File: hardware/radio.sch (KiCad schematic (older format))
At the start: 80 parts, among them J1 JCLK, P2 JLED1, U1 G144A12, U3V3t1V8 NCP1117ST18T3G, U5V0t3V3 NCP1117ST33T3G

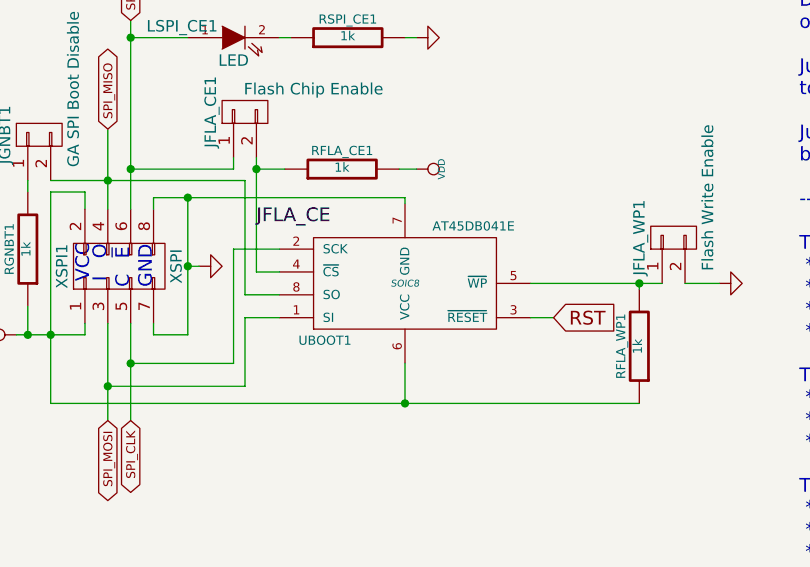
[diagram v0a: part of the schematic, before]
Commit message: Adding SATA PCB module.
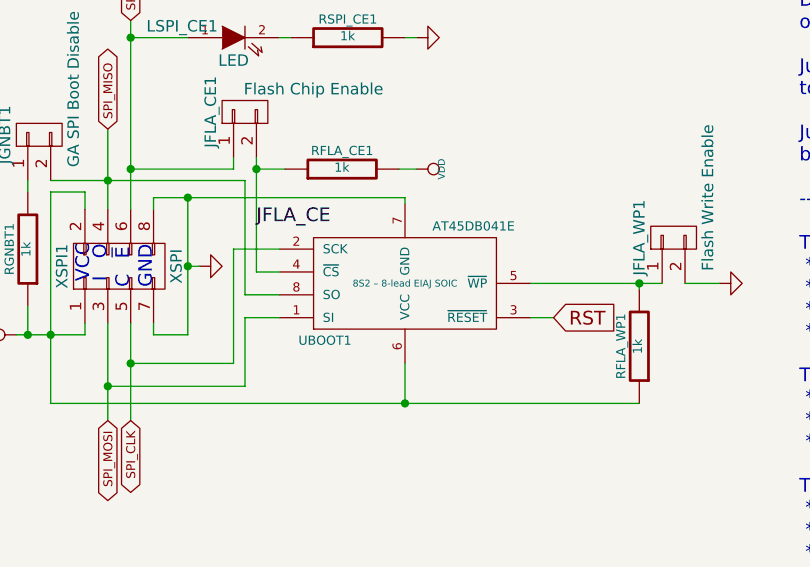
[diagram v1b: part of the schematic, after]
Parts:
- AN2: footprint (none) -> Pin_Headers:Pin_Header_Straight_1x03
- CPWR1: footprint (none) -> Connect:BARREL_JACK
- JFLA_CE1, JFLA_WP1, JGNBT1: footprint (none) -> Pin_Headers:Pin_Header_Straight_1x02
- RFLA_CE1, RFLA_WP1, RGNBT1, RLB1, ROE1, RSPI_CE1, RUB1: footprint (none) -> Resistors_SMD:R_0603
- U5V0t3V3: footprint (none) -> SMD_Packages:SOT-223
- UBOOT1: footprint SOIC8 -> SMD_Packages:SOIC-8-N
- XMEM1: footprint (none) -> tssop2-44:TSSOPII-44_0.8mmPitch
- XSPI1: footprint (none) -> Pin_Headers:Pin_Header_Straight_1x04
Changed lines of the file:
@@
 F 0 "XSPI1" H 6525 15525 50  0000 C CNN
 F 1 "XSPI" H 6525 15025 50  0000 C CNN
-F 2 "" H 6525 14075 60  0000 C CNN
+F 2 "Pin_Headers:Pin_Header_Straight_1x04" H 6525 14075 60  0001 C CNN
 F 3 "" H 6525 14075 60  0000 C CNN
 	1    6525 15275
@@
 F 0 "UBOOT1" H 7425 15600 40  0000 C CNN
 F 1 "AT45DB041E" H 8075 15100 40  0000 C CNN
-F 2 "SOIC8" H 7775 15350 30  0000 C CIN
-F 3 "" H 7775 15350 60  0000 C CNN
+F 2 "SMD_Packages:SOIC-8-N" H 7775 15350 30  0001 C CIN
+F 3 "8S2 – 8-lead EIAJ SOIC" H 7775 15350 30  0000 C CNN
 	1    7775 15350
 	1    0    0    1
@@
 F 0 "JFLA_WP1" H 8950 15300 50  0000 C CNN
 F 1 "Flash Write Enable" H 9125 15000 50  0000 C CNN
-F 2 "" H 8950 15150 60  0000 C CNN
+F 2 "Pin_Headers:Pin_Header_Straight_1x02" H 8950 15150 60  0001 C CNN
 F 3 "" H 8950 15150 60  0000 C CNN
 	1    8950 15150
@@
 F 0 "RFLA_WP1" V 8880 15625 40  0000 C CNN
 F 1 "1k" V 8807 15626 40  0000 C CNN
-F 2 "" V 8730 15625 30  0000 C CNN
+F 2 "Resistors_SMD:R_0603" V 8730 15625 30  0001 C CNN
 F 3 "" H 8800 15625 30  0000 C CNN
 	1    8800 15625
@@
 F 0 "AN2" H 30275 6900 50  0000 C CNN
 F 1 "CONN_01X03" V 30375 6700 50  0000 C CNN
-F 2 "" H 30275 6700 60  0000 C CNN
+F 2 "Pin_Headers:Pin_Header_Straight_1x03" H 30275 6700 60  0001 C CNN
 F 3 "" H 30275 6700 60  0000 C CNN
 	1    30275 6700
@@
 F 0 "CPWR1" H 28100 5750 60  0000 C CNN
 F 1 "BARREL_JACK" H 28100 5300 60  0000 C CNN
-F 2 "" H 28100 5500 60  0000 C CNN
+F 2 "Connect:BARREL_JACK" H 28100 5500 60  0001 C CNN
 F 3 "" H 28100 5500 60  0000 C CNN
 	1    28100 5500
@@
 F 0 "U5V0t3V3" H 26975 5700 40  0000 C CNN
 F 1 "NCP1117ST33T3G" H 26975 5650 40  0000 C CNN
-F 2 "" H 26975 5450 60  0000 C CNN
+F 2 "SMD_Packages:SOT-223" H 26975 5450 60  0001 C CNN
 F 3 "" H 26975 5450 60  0000 C CNN
 	1    26975 5450
@@
 F 0 "XMEM1" H 4500 8250 50  0000 C CNN
 F 1 "IS62/65WV51216E(A|B)LL" V 4500 7100 50  0000 C CNN
-F 2 "" H 4500 6200 60  0000 C CNN
+F 2 "tssop2-44:TSSOPII-44_0.8mmPitch" H 4500 6200 60  0001 C CNN
 F 3 "" H 4500 6200 60  0000 C CNN
 	1    4500 7100
@@
 F 0 "RUB1" V 5125 8600 40  0000 C CNN
 F 1 "1K" V 5082 8851 40  0000 C CNN
-F 2 "" V 5005 8850 30  0000 C CNN
+F 2 "Resistors_SMD:R_0603" V 5005 8850 30  0001 C CNN
 F 3 "" H 5075 8850 30  0000 C CNN
 	1    5075 8850
@@
 F 0 "RLB1" V 5125 8700 40  0000 C CNN
 F 1 "1K" V 5082 8951 40  0000 C CNN
-F 2 "" V 5005 8950 30  0000 C CNN
+F 2 "Resistors_SMD:R_0603" V 5005 8950 30  0001 C CNN
 F 3 "" H 5075 8950 30  0000 C CNN
 	1    5075 8950
@@
 F 0 "ROE1" V 5125 8500 40  0000 C CNN
 F 1 "1K" V 5082 8751 40  0000 C CNN
-F 2 "" V 5005 8750 30  0000 C CNN
+F 2 "Resistors_SMD:R_0603" V 5005 8750 30  0001 C CNN
 F 3 "" H 5075 8750 30  0000 C CNN
 	1    5075 8750
@@
 F 0 "AN0" H 31925 6650 50  0000 C CNN
 F 1 "Analog 709 / 713" V 32225 6175 50  0000 C CNN
-F 2 "" H 32275 6150 60  0000 C CNN
+F 2 "" H 32275 6150 60  0001 C CNN
 F 3 "" H 32275 6150 60  0000 C CNN
 	1    31925 6150
@@
 F 0 "AN1" H 31925 7625 50  0000 C CNN
 F 1 "Analog 617 / 117" V 32225 7150 50  0000 C CNN
-F 2 "" H 32275 7125 60  0000 C CNN
+F 2 "" H 32275 7125 60  0001 C CNN
 F 3 "" H 32275 7125 60  0000 C CNN
 	1    31925 7125
@@
 F 0 "JGNBT1" H 6175 14850 50  0000 C CNN
 F 1 "GA SPI Boot Disable" H 6375 14550 50  0000 C CNN
-F 2 "" H 6175 14700 60  0000 C CNN
+F 2 "Pin_Headers:Pin_Header_Straight_1x02" H 6175 14700 60  0001 C CNN
 F 3 "" H 6175 14700 60  0000 C CNN
 	1    6175 14700
@@
 F 0 "RGNBT1" V 6205 15200 40  0000 C CNN
 F 1 "1k" V 6132 15201 40  0000 C CNN
-F 2 "" V 6055 15200 30  0000 C CNN
+F 2 "Resistors_SMD:R_0603" V 6055 15200 30  0001 C CNN
 F 3 "" H 6125 15200 30  0000 C CNN
 	1    6125 15200
@@
 F 0 "RFLA_CE1" V 7580 14850 40  0000 C CNN
 F 1 "1k" V 7507 14851 40  0000 C CNN
-F 2 "" V 7430 14850 30  0000 C CNN
+F 2 "Resistors_SMD:R_0603" V 7430 14850 30  0001 C CNN
 F 3 "" H 7500 14850 30  0000 C CNN
 	1    7500 14850
@@
 F 0 "JFLA_CE1" H 7075 14750 50  0000 C CNN
 F 1 "Flash Chip Enable" V 7175 14300 50  0000 C CNN
-F 2 "" H 7075 14600 60  0000 C CNN
+F 2 "Pin_Headers:Pin_Header_Straight_1x02" H 7075 14600 60  0001 C CNN
 F 3 "" H 7075 14600 60  0000 C CNN
 	1    7075 14600
@@
 F 0 "RSPI_CE1" V 7605 14275 40  0000 C CNN
 F 1 "1k" V 7532 14276 40  0000 C CNN
-F 2 "" V 7455 14275 30  0000 C CNN
+F 2 "Resistors_SMD:R_0603" V 7455 14275 30  0001 C CNN
 F 3 "" H 7525 14275 30  0000 C CNN
 	1    7525 14275

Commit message: Back to pin headers rather than SATA connectors.
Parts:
- removed AN0: Analog 709 / 713, symbol Custom-SATA-Output
- removed AN1: Analog 617 / 117, symbol Custom-SATA-Output
- removed AN2: CONN_01X03, Pin_Headers:Pin_Header_Straight_1x03, symbol CONN_01X03
- added AN0, AN1: CONN_01X09, Pin_Headers:Pin_Header_Straight_1x09, symbol CONN_01X09
- added AN2: CONN_01X05, Pin_Headers:Pin_Header_Straight_1x03, symbol CONN_01X05
- added AT0: Analog Timing, Pin_Headers:Pin_Header_Straight_1x02, symbol CONN_01X02
- added C4, C5, C6, C7, C8: 100nF, SMD_Packages:SMD-0603, symbol C
- C1: renamed from C3; value C -> 100nF
- C2: renamed from C4; value C -> 100nF
- C3: renamed from C5; value C -> 100nF
- CLVL1: renamed from C1; value C -> 100nF
- CVIN33, CVIN5V0, CVOUT1V8, CVOUT3V3: value C -> 10uF; footprint SMD_Packages:SMD-0603 -> SMD_Packages:SMD-0805
- JLED1: renamed from P2; value JLED1 -> Debug Led Jumpers
- RL1V8, RLED1, RLED2, RLED3, RRST2: value 500 -> 1k
- renumbered C2 to CID1, R4 to RLVL1, CDO1 to XDO1, CPWR1 to XPWR1, CRPI1 to XRPI1, CSYNC1 to XSYNC1
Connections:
- wire segments 495 -> 512
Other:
- note removed: "SATA connectors\nA pins == analog in (RX)\nB pins == analog out (TX)"
- moved on the sheet: C1, C2, C3, RLVL1

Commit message: Fixing XSPI connector.
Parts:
- XSPI1: footprint Pin_Headers:Pin_Header_Straight_1x04 -> Pin_Headers:Pin_Header_Straight_2x04
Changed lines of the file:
@@
 F 0 "XSPI1" H 6525 15525 50  0000 C CNN
 F 1 "XSPI" H 6525 15025 50  0000 C CNN
-F 2 "Pin_Headers:Pin_Header_Straight_1x04" H 6525 14075 60  0001 C CNN
+F 2 "Pin_Headers:Pin_Header_Straight_2x04" H 6525 14075 60  0001 C CNN
 F 3 "" H 6525 14075 60  0000 C CNN
 	1    6525 15275

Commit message: Temporary commit for netlist import.
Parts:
- AN2: footprint Pin_Headers:Pin_Header_Straight_1x03 -> Pin_Headers:Pin_Header_Straight_1x05
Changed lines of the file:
@@
 F 0 "AN2" H 31925 7150 50  0000 C CNN
 F 1 "CONN_01X05" V 32025 6850 50  0000 C CNN
-F 2 "Pin_Headers:Pin_Header_Straight_1x03" H 31925 6850 60  0001 C CNN
+F 2 "Pin_Headers:Pin_Header_Straight_1x05" H 31925 6850 60  0001 C CNN
 F 3 "" H 31925 6850 60  0000 C CNN
 	1    31925 6850

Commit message: More work.
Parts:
- RFLA_CE1, RFLA_WP1, RGNBT1, RID_SC1, RID_SD1, RL1V8, RL3V3, RLB1, RLED1, RLED2, RLED3, RLVL1, ROE1, RPU10, RPU11, RPU12, RPU13, RPU14, RPU15, RPU16, RPU17, RPU18, RPU19, RPU20, RPU21, RPU22, RPU3, RPU4, RPU5, RPU6, RPU7, RPU8, RPU9, RRST1, RRST2, RSCL1, RSDA1, RSPI_CE1, RUB1, RWR1: footprint Resistors_SMD:R_0603 -> rsmd:R_0603
- XRST1: footprint Connect:GS2 -> SMD_Packages:SMD-1206

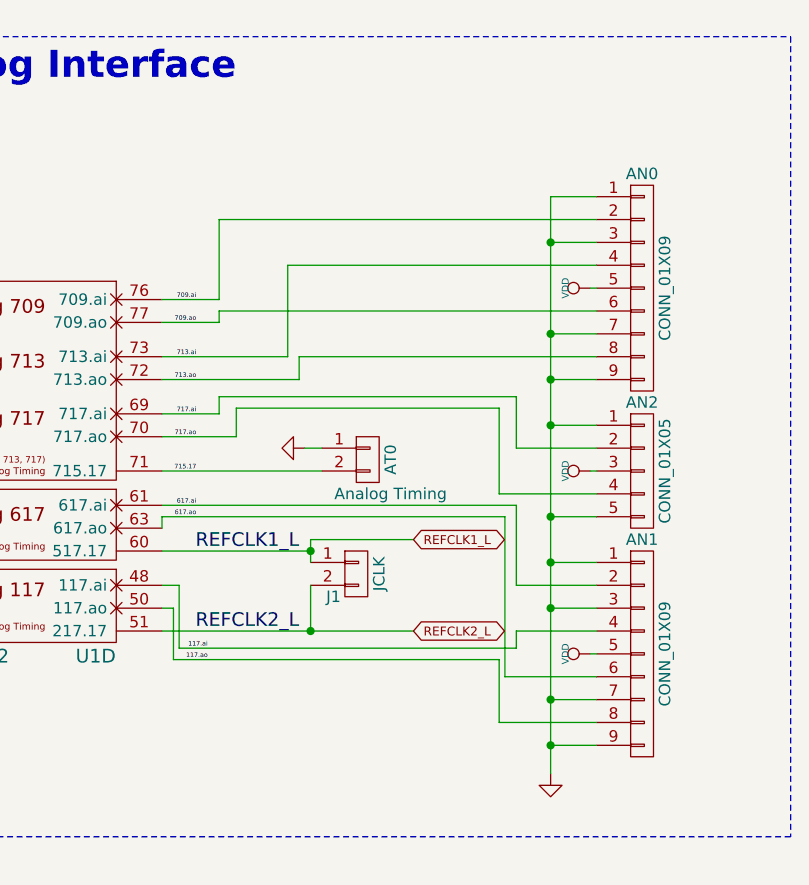
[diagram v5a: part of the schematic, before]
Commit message: Reorganising the Analog header for easier routing.
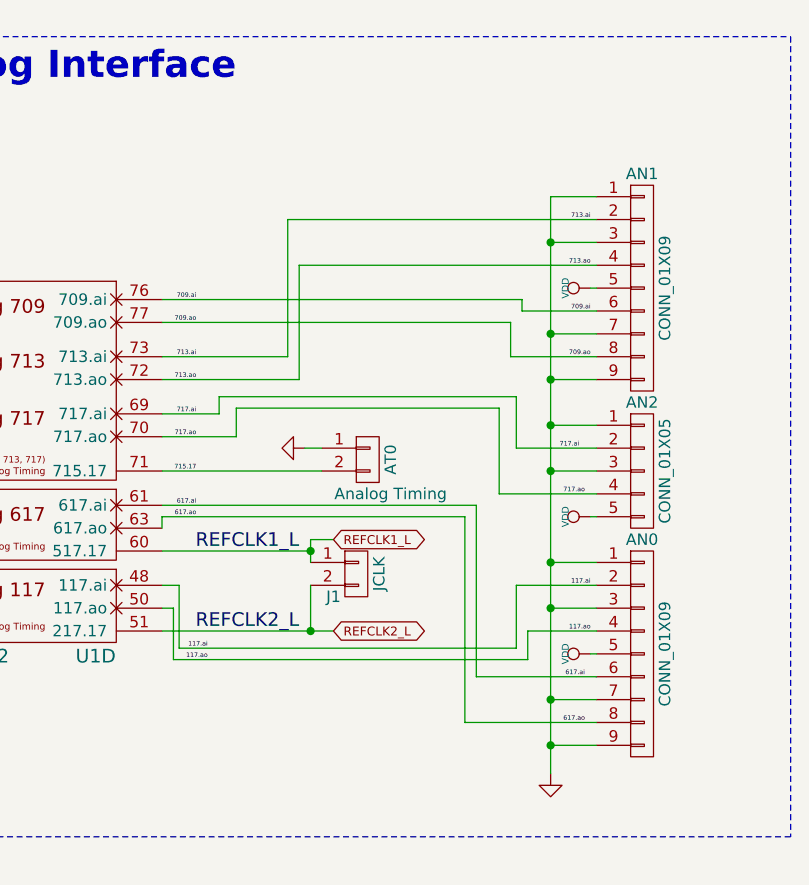
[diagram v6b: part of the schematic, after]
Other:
- moved on the sheet: AN0, AN1
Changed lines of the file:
@@
 	1    0    0    -1
 $EndComp
-Text GLabel 30925 7150 2    39   BiDi ~ 0
+Text GLabel 30575 7150 2    39   BiDi ~ 0
 REFCLK1_L
-Text GLabel 30925 7550 2    39   BiDi ~ 0
+Text GLabel 30575 7550 2    39   BiDi ~ 0
 REFCLK2_L
 Text GLabel 1850 10200 2    39   Input ~ 0
@@
 L CONN_01X09 AN0
 U 1 1 5455E7B5
-P 31925 6050
-F 0 "AN0" H 31925 6550 50  0000 C CNN
-F 1 "CONN_01X09" V 32025 6050 50  0000 C CNN
-F 2 "Pin_Headers:Pin_Header_Straight_1x09" H 31925 6050 60  0001 C CNN
-F 3 "" H 31925 6050 60  0000 C CNN
-	1    31925 6050
+P 31925 7650
+F 0 "AN0" H 31925 8150 50  0000 C CNN
+F 1 "CONN_01X09" V 32025 7650 50  0000 C CNN
+F 2 "Pin_Headers:Pin_Header_Straight_1x09" H 31925 7650 60  0001 C CNN
+F 3 "" H 31925 7650 60  0000 C CNN
+	1    31925 7650
 	1    0    0    -1
 $EndComp
@@
 L CONN_01X09 AN1
 U 1 1 54565953
-P 31925 7650
-F 0 "AN1" H 31925 8150 50  0000 C CNN
-F 1 "CONN_01X09" V 32025 7650 50  0000 C CNN
-F 2 "Pin_Headers:Pin_Header_Straight_1x09" H 31925 7650 60  0001 C CNN
-F 3 "" H 31925 7650 60  0000 C CNN
-	1    31925 7650
+P 31925 6050
+F 0 "AN1" H 31925 6550 50  0000 C CNN
+F 1 "CONN_01X09" V 32025 6050 50  0000 C CNN
+F 2 "Pin_Headers:Pin_Header_Straight_1x09" H 31925 6050 60  0001 C CNN
+F 3 "" H 31925 6050 60  0000 C CNN
+	1    31925 6050
 	1    0    0    -1
 $EndComp
@@
 L VDD #PWR031
 U 1 1 5456ADCD
-P 31700 6850
-F 0 "#PWR031" H 31700 6950 30  0001 C CNN
-F 1 "VDD" H 31700 6960 30  0000 C CNN
-F 2 "" H 31700 6850 60  0000 C CNN
-F 3 "" H 31700 6850 60  0000 C CNN
-	1    31700 6850
+P 31700 7050
+F 0 "#PWR031" H 31700 7150 30  0001 C CNN
+F 1 "VDD" H 31700 7160 30  0000 C CNN
+F 2 "" H 31700 7050 60  0000 C CNN
+F 3 "" H 31700 7050 60  0000 C CNN
+	1    31700 7050
 	0    -1   -1   0
 $EndComp
@@
 	0    -1   -1   0
 $EndComp
+$Comp
+L CONN_01X02 AT0
+U 1 1 54573888
+P 30725 6800
+F 0 "AT0" V 30825 6800 50  0000 C CNN
+F 1 "Analog Timing" H 30825 6650 50  0000 C CNN
+F 2 "Pin_Headers:Pin_Header_Straight_1x02" H 30725 6800 60  0001 C CNN
+F 3 "" H 30725 6800 60  0000 C CNN
+	1    30725 6800
+	1    0    0    -1
+$EndComp
+$Comp
+L GND #PWR033
+U 1 1 54574DD7
+P 30450 6750
+F 0 "#PWR033" H 30450 6750 30  0001 C CNN
+F 1 "GND" H 30450 6680 30  0001 C CNN
+F 2 "" H 30450 6750 60  0000 C CNN
+F 3 "" H 30450 6750 60  0000 C CNN
+	1    30450 6750
+	0    1    1    0
+$EndComp
+$Comp
+L C C8
+U 1 1 5457D457
+P 25425 8050
+F 0 "C8" H 25425 8150 40  0000 L CNN
+F 1 "100nF" H 25431 7965 40  0000 L CNN
+F 2 "SMD_Packages:SMD-0603" H 25463 7900 30  0001 C CNN
+F 3 "" H 25425 8050 60  0000 C CNN
+	1    25425 8050
+	-1   0    0    1
+$EndComp
+$Comp
+L C C7
+U 1 1 5457D521
+P 25625 8050
+F 0 "C7" H 25625 8150 40  0000 L CNN
+F 1 "100nF" H 25631 7965 40  0000 L CNN
+F 2 "SMD_Packages:SMD-0603" H 25663 7900 30  0001 C CNN
+F 3 "" H 25625 8050 60  0000 C CNN
+	1    25625 8050
+	-1   0    0    1
+$EndComp
+$Comp
+L C C6
+U 1 1 5457D5D6
+P 25825 8050
+F 0 "C6" H 25825 8150 40  0000 L CNN
+F 1 "100nF" H 25831 7965 40  0000 L CNN
+F 2 "SMD_Packages:SMD-0603" H 25863 7900 30  0001 C CNN
+F 3 "" H 25825 8050 60  0000 C CNN
+	1    25825 8050
+	-1   0    0    1
+$EndComp
+$Comp
+L C C5
+U 1 1 5457D67A
+P 26025 8050
+F 0 "C5" H 26025 8150 40  0000 L CNN
+F 1 "100nF" H 26031 7965 40  0000 L CNN
+F 2 "SMD_Packages:SMD-0603" H 26063 7900 30  0001 C CNN
+F 3 "" H 26025 8050 60  0000 C CNN
+	1    26025 8050
+	-1   0    0    1
+$EndComp
+$Comp
+L C C4
+U 1 1 5457D912
+P 26025 7550
+F 0 "C4" H 26025 7650 40  0000 L CNN
+F 1 "100nF" H 26031 7465 40  0000 L CNN
+F 2 "SMD_Packages:SMD-0603" H 26063 7400 30  0001 C CNN
+F 3 "" H 26025 7550 60  0000 C CNN
+	1    26025 7550
+	1    0    0    -1
+$EndComp
+Text Label 31700 7550 2    20   ~ 0
+117.ao
+Text Label 31700 7350 2    20   ~ 0
+117.ai
+Text Label 31675 7950 2    20   ~ 0
+617.ao
+Text Label 31675 7750 2    20   ~ 0
+617.ai
+Text Label 31675 6950 2    20   ~ 0
+717.ao
+Text Label 31650 6750 2    20   ~ 0
+717.ai
+Text Label 31700 6150 2    20   ~ 0
+709.ai
+Text Label 31700 6350 2    20   ~ 0
+709.ao
+Text Label 31700 5750 2    20   ~ 0
+713.ai
+Text Label 31700 5950 2    20   ~ 0
+713.ao
 Wire Wire Line
 	25075 6150 25275 6150
@@
 	29825 7200 30475 7200
 Wire Wire Line
-	29825 7550 30925 7550
+	29825 7550 30575 7550
 Wire Wire Line
 	30475 7150 30475 7250
@@
 	30475 7550 30475 7350
 Wire Wire Line
-	30475 7150 30925 7150
+	30475 7150 30575 7150
 Connection ~ 30475 7200
 Connection ~ 30475 7550
@@
 Connection ~ 6575 14850
 Wire Wire Line
-	30075 5750 30075 6100
-Wire Wire Line
-	30075 6100 29825 6100
-Wire Wire Line
-	29825 6200 30075 6200
+	29825 6100 31400 6100
+Wire Wire Line
+	29825 6200 31350 6200
 Wire Wire Line
 	30375 6350 29825 6350
 Wire Wire Line
-	30375 5950 30375 6350
-Wire Wire Line
-	29825 6450 30425 6450
-Wire Wire Line
-	29825 7000 31375 7000
+	30425 6450 29825 6450
+Wire Wire Line
+	29825 7000 31200 7000
 Wire Wire Line
 	29825 7450 29875 7450
@@
 	29875 7450 29875 7675
 Wire Wire Line
-	29875 7675 31300 7675
-Wire Wire Line
-	31375 7550 31375 7625
+	29875 7675 31425 7675
 Wire Wire Line
 	31375 7625 29900 7625
@@
 	29825 7100 29825 7050
 Wire Wire Line
-	29825 7050 31325 7050
+	29825 7050 31150 7050
 Wire Wire Line
 	29825 6600 30075 6600
@@
 Wire Wire Line
 	29825 6850 30525 6850
-Wire Wire Line
-	31325 7050 31325 7750
 Wire Wire Line
 	27375 5400 27800 5400
@@
 	7775 14275 7825 14275
 Wire Wire Line
-	30375 5950 31725 5950
-Wire Wire Line
 	31725 5850 31525 5850
 Connection ~ 31525 5850
 Wire Wire Line
-	31725 5750 30075 5750
-Wire Wire Line
 	31525 5650 31525 8175
 Wire Wire Line
@@
 	31700 6050 31725 6050
 Wire Wire Line
-	31725 6150 30075 6150
-Wire Wire Line
-	30075 6150 30075 6200
-Wire Wire Line
 	31525 6250 31725 6250
-Wire Wire Line
-	31725 6350 30425 6350
-Wire Wire Line
-	30425 6350 30425 6450
 Wire Wire Line
 	31525 6450 31725 6450
 Connection ~ 31525 6250
 Wire Wire Line
-	31375 7000 31375 7350
-Wire Wire Line
-	31375 7350 31725 7350
-Wire Wire Line
-	31300 7675 31300 7950
-Wire Wire Line
-	31300 7950 31725 7950
-Wire Wire Line
-	31325 7750 31725 7750
-Wire Wire Line
-	31375 7550 31725 7550
-Wire Wire Line
-	31700 6850 31725 6850
-Wire Wire Line
 	31525 8050 31725 8050
 Connection ~ 31525 6450
@@
 	31525 7850 31725 7850
 Connection ~ 31525 7850
-Wire Wire Line
-	31725 7050 31525 7050
-Connection ~ 31525 7050
-Wire Wire Line
-	31725 6650 31525 6650
-Connection ~ 31525 6650
 Connection ~ 31525 8050
 Wire Wire Line
@@
 	31725 7450 31525 7450
 Connection ~ 31525 7450
-$Comp
-L CONN_01X02 AT0
-U 1 1 54573888
-P 30725 6800
-F 0 "AT0" V 30825 6800 50  0000 C CNN
-F 1 "Analog Timing" H 30825 6650 50  0000 C CNN
-F 2 "Pin_Headers:Pin_Header_Straight_1x02" H 30725 6800 60  0001 C CNN
-F 3 "" H 30725 6800 60  0000 C CNN
-	1    30725 6800
-	1    0    0    -1
-$EndComp
 Wire Wire Line
 	30075 6600 30075 6525
@@
 	31375 6525 31375 6750
 Wire Wire Line
-	31375 6750 31725 6750
-Wire Wire Line
-	31725 6950 31300 6950
-Wire Wire Line
 	31300 6950 31300 6575
 Wire Wire Line
@@
 Wire Wire Line
 	30150 6575 30150 6700
-$Comp
-L GND #PWR033
-U 1 1 54574DD7
-P 30450 6750
-F 0 "#PWR033" H 30450 6750 30  0001 C CNN
-F 1 "GND" H 30450 6680 30  0001 C CNN
-F 2 "" H 30450 6750 60  0000 C CNN
-F 3 "" H 30450 6750 60  0000 C CNN
-	1    30450 6750
-	0    1    1    0
-$EndComp
 Wire Wire Line
 	30450 6750 30525 6750
-$Comp
-L C C8
-U 1 1 5457D457
-P 25425 8050
-F 0 "C8" H 25425 8150 40  0000 L CNN
-F 1 "100nF" H 25431 7965 40  0000 L CNN
-F 2 "SMD_Packages:SMD-0603" H 25463 7900 30  0001 C CNN
-F 3 "" H 25425 8050 60  0000 C CNN
-	1    25425 8050
-	-1   0    0    1
-$EndComp
-$Comp
-L C C7
-U 1 1 5457D521
-P 25625 8050
-F 0 "C7" H 25625 8150 40  0000 L CNN
-F 1 "100nF" H 25631 7965 40  0000 L CNN
-F 2 "SMD_Packages:SMD-0603" H 25663 7900 30  0001 C CNN
-F 3 "" H 25625 8050 60  0000 C CNN
-	1    25625 8050
-	-1   0    0    1
-$EndComp
-$Comp
-L C C6
-U 1 1 5457D5D6
-P 25825 8050
-F 0 "C6" H 25825 8150 40  0000 L CNN
-F 1 "100nF" H 25831 7965 40  0000 L CNN
-F 2 "SMD_Packages:SMD-0603" H 25863 7900 30  0001 C CNN
-F 3 "" H 25825 8050 60  0000 C CNN
-	1    25825 8050
-	-1   0    0    1
-$EndComp
-$Comp
-L C C5
-U 1 1 5457D67A
-P 26025 8050
-F 0 "C5" H 26025 8150 40  0000 L CNN
-F 1 "100nF" H 26031 7965 40  0000 L CNN
-F 2 "SMD_Packages:SMD-0603" H 26063 7900 30  0001 C CNN
-F 3 "" H 26025 8050 60  0000 C CNN
-	1    26025 8050
-	-1   0    0    1
-$EndComp
-$Comp
-L C C4
-U 1 1 5457D912
-P 26025 7550
-F 0 "C4" H 26025 7650 40  0000 L CNN
-F 1 "100nF" H 26031 7465 40  0000 L CNN
-F 2 "SMD_Packages:SMD-0603" H 26063 7400 30  0001 C CNN
-F 3 "" H 26025 7550 60  0000 C CNN
-	1    26025 7550
-	1    0    0    -1
-$EndComp
 Wire Wire Line
 	26025 7300 26025 7350
@@
 Connection ~ 25825 7800
 Connection ~ 26025 7800
+Wire Wire Line
+	31375 7625 31375 7350
+Wire Wire Line
+	31375 7350 31725 7350
+Wire Wire Line
+	31425 7675 31425 7550
+Wire Wire Line
+	31425 7550 31725 7550
+Wire Wire Line
+	31150 7050 31150 7950
+Wire Wire Line
+	31150 7950 31725 7950
+Wire Wire Line
+	31200 7000 31200 7750
+Wire Wire Line
+	31200 7750 31725 7750
+Wire Wire Line
+	31725 6650 31525 6650
+Connection ~ 31525 6650
+Wire Wire Line
+	31300 6950 31725 6950
+Wire Wire Line
+	31375 6750 31725 6750
+Wire Wire Line
+	31725 6850 31525 6850
+Connection ~ 31525 6850
+Wire Wire Line
+	31725 7050 31700 7050
+Wire Wire Line
+	31400 6100 31400 6150
+Wire Wire Line
+	31400 6150 31725 6150
+Wire Wire Line
+	31350 6200 31350 6350
+Wire Wire Line
+	31350 6350 31725 6350
+Wire Wire Line
+	30375 6350 30375 5750
+Wire Wire Line
+	30375 5750 31725 5750
+Wire Wire Line
+	30425 5950 31725 5950
+Wire Wire Line
+	30425 5950 30425 6450
 $EndSCHEMATC
